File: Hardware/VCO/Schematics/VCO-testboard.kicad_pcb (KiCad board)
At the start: 2 copper layers, 29 parts, among them J1 Conn_01x02, J2 Conn_01x02, J3 Conn_01x02, J4 Conn_01x02, U1 LM358

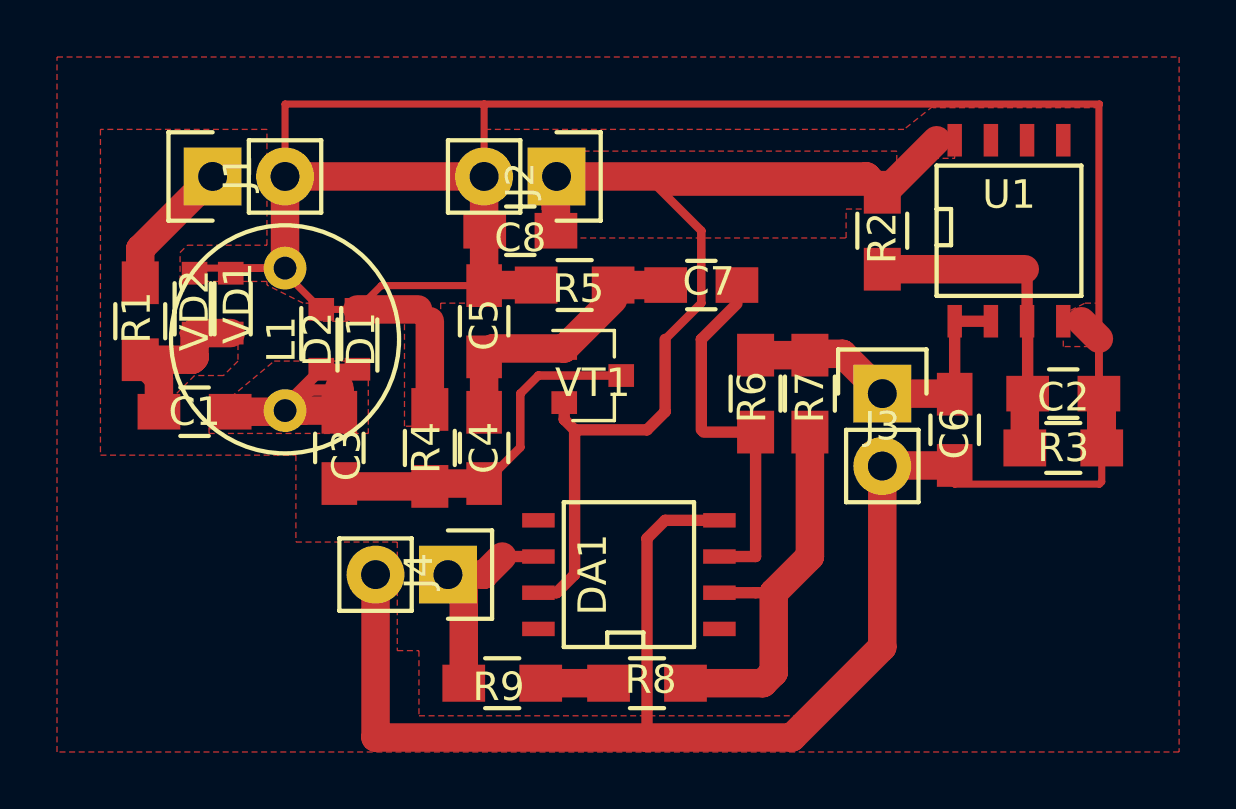
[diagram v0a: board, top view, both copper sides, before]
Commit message: Changed layout a bit
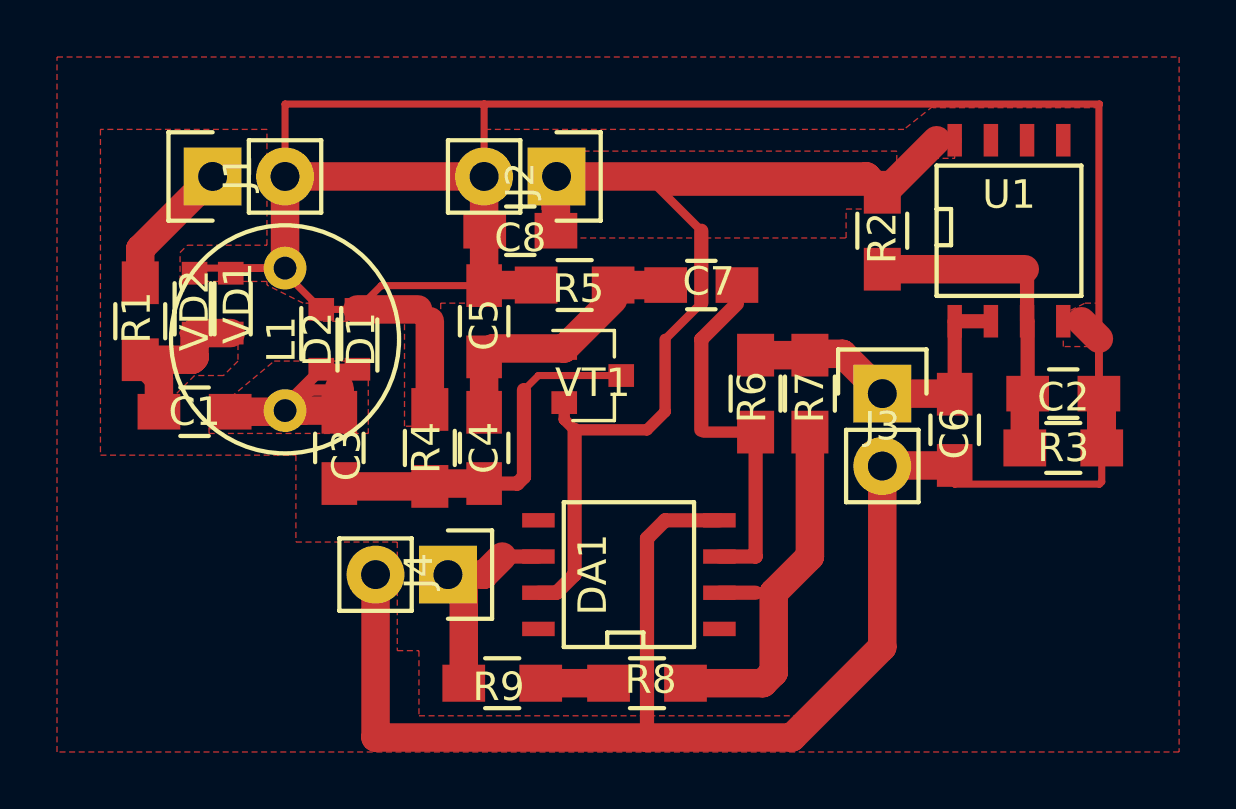
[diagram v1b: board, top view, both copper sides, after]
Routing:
- net Net-(C3-Pad1): track 12.6 -> 13.3 mm
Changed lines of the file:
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@@
     (thickness 1.6)
     (drawings 4)
-    (tracks 163)
+    (tracks 164)
     (zones 0)
     (modules 29)
@@
   )
   (setup
-    (last_trace_width 1)
+    (last_trace_width 0.5)
     (user_trace_width 0.3)
     (user_trace_width 0.4)
+    (user_trace_width 0.5)
     (user_trace_width 1)
     (trace_clearance 0.2)
@@
   (segment (start 16.53 24.23) (end 16.53 25.4) (width 0.25) (layer F.Cu) (net 2))
   (segment (start 17.365 22.64) (end 19.05 22.64) (width 0.25) (layer F.Cu) (net 2))
-  (segment (start 46.99 22.225) (end 46.99 20.32) (width 0.4) (layer F.Cu) (net 3))
+  (segment (start 46.99 22.225) (end 46.99 20.32) (width 0.5) (layer F.Cu) (net 3))
   (segment (start 46.91 20.4) (end 41.91 20.4) (width 1) (layer F.Cu) (net 3))
   (segment (start 46.99 20.32) (end 46.91 20.4) (width 0.25) (layer F.Cu) (net 3))
-  (segment (start 47.01 24.765) (end 47.01 22.245) (width 0.4) (layer F.Cu) (net 3))
+  (segment (start 47.01 24.765) (end 47.01 22.245) (width 0.5) (layer F.Cu) (net 3))
   (segment (start 47.01 22.245) (end 46.99 22.225) (width 0.25) (layer F.Cu) (net 3))
   (segment (start 46.91 24.665) (end 46.91 26.67) (width 1) (layer F.Cu) (net 3))
@@
   (segment (start 24.13 31.115) (end 24.13 36.83) (width 1) (layer F.Cu) (net 4))
   (segment (start 24.13 36.83) (end 33.655 36.83) (width 1) (layer F.Cu) (net 4))
-  (segment (start 36.195 29.21) (end 34.29 29.21) (width 0.4) (layer F.Cu) (net 4))
+  (segment (start 36.195 29.21) (end 34.29 29.21) (width 0.5) (layer F.Cu) (net 4))
   (segment (start 41.91 33.655) (end 41.91 27.305) (width 1) (layer F.Cu) (net 4))
   (segment (start 38.735 36.83) (end 41.91 33.655) (width 1) (layer F.Cu) (net 4))
   (segment (start 33.655 36.83) (end 38.735 36.83) (width 1) (layer F.Cu) (net 4))
-  (segment (start 33.655 29.845) (end 33.655 36.83) (width 0.4) (layer F.Cu) (net 4))
-  (segment (start 34.29 29.21) (end 33.655 29.845) (width 0.4) (layer F.Cu) (net 4))
+  (segment (start 33.655 29.845) (end 33.655 36.83) (width 0.5) (layer F.Cu) (net 4))
+  (segment (start 34.29 29.21) (end 33.655 29.845) (width 0.5) (layer F.Cu) (net 4))
   (segment (start 27.94 14.605) (end 49.53 14.605) (width 0.25) (layer F.Cu) (net 4))
   (segment (start 49.51 14.625) (end 49.51 24.765) (width 0.25) (layer F.Cu) (net 4))
@@
   (segment (start 22.225 21.81) (end 20.955 20.54) (width 0.25) (layer F.Cu) (net 4))
   (segment (start 20.955 20.54) (end 20.955 20.36064) (width 0.25) (layer F.Cu) (net 4))
-  (segment (start 32.75 24.13) (end 29.845 24.13) (width 0.3) (layer F.Cu) (net 5))
-  (segment (start 29.21 26.65) (end 27.94 27.92) (width 0.3) (layer F.Cu) (net 5))
-  (segment (start 29.21 24.765) (end 29.21 26.65) (width 0.3) (layer F.Cu) (net 5))
-  (segment (start 29.845 24.13) (end 29.21 24.765) (width 0.3) (layer F.Cu) (net 5))
+  (segment (start 32.75 24.13) (end 29.845 24.13) (width 0.25) (layer F.Cu) (net 5) (status 400000))
+  (segment (start 29.103 27.92) (end 27.94 27.92) (width 0.5) (layer F.Cu) (net 5) (status 800000))
+  (segment (start 29.337 27.686) (end 29.103 27.92) (width 0.5) (layer F.Cu) (net 5))
+  (segment (start 29.337 24.638) (end 29.337 27.686) (width 0.5) (layer F.Cu) (net 5))
+  (segment (start 29.845 24.13) (end 29.337 24.638) (width 0.25) (layer F.Cu) (net 5))
   (segment (start 27.94 27.92) (end 26.135 27.92) (width 1) (layer F.Cu) (net 5))
   (segment (start 26.135 27.92) (end 26.035 28.02) (width 0.25) (layer F.Cu) (net 5))
@@
   (segment (start 39.45 23.495) (end 39.37 23.415) (width 0.25) (layer F.Cu) (net 7))
   (segment (start 39.37 23.415) (end 37.465 23.415) (width 0.25) (layer F.Cu) (net 7))
-  (segment (start 44.45 24.785) (end 44.45 22.225) (width 0.4) (layer F.Cu) (net 7))
+  (segment (start 44.45 24.785) (end 44.45 22.225) (width 0.5) (layer F.Cu) (net 7))
   (segment (start 44.45 24.785) (end 41.93 24.785) (width 0.25) (layer F.Cu) (net 7))
   (segment (start 41.93 24.785) (end 41.91 24.765) (width 0.25) (layer F.Cu) (net 7))
-  (segment (start 45.72 22.225) (end 44.45 22.225) (width 0.4) (layer F.Cu) (net 7))
-  (segment (start 36.195 30.48) (end 37.465 30.48) (width 0.4) (layer F.Cu) (net 8))
-  (segment (start 37.465 30.48) (end 37.465 26.115) (width 0.4) (layer F.Cu) (net 8))
+  (segment (start 45.72 22.225) (end 44.45 22.225) (width 0.5) (layer F.Cu) (net 7))
+  (segment (start 36.195 30.48) (end 37.465 30.48) (width 0.5) (layer F.Cu) (net 8))
+  (segment (start 37.465 30.48) (end 37.465 26.115) (width 0.5) (layer F.Cu) (net 8))
   (segment (start 36.81 20.955) (end 36.81 21.61) (width 0.25) (layer F.Cu) (net 8))
   (segment (start 35.64 26.115) (end 37.465 26.115) (width 0.4) (layer F.Cu) (net 8))
   (segment (start 35.56 26.035) (end 35.64 26.115) (width 0.3) (layer F.Cu) (net 8))
-  (segment (start 35.56 22.86) (end 35.56 26.035) (width 0.4) (layer F.Cu) (net 8))
-  (segment (start 36.81 21.61) (end 35.56 22.86) (width 0.4) (layer F.Cu) (net 8))
+  (segment (start 35.56 22.86) (end 35.56 26.035) (width 0.5) (layer F.Cu) (net 8))
+  (segment (start 36.81 21.61) (end 35.56 22.86) (width 0.5) (layer F.Cu) (net 8))
+  (segment (start 31.115 26.035) (end 33.655 26.035) (width 0.4) (layer F.Cu) (net 9))
+  (segment (start 35.56 19.05) (end 33.655 17.145) (width 0.3) (layer F.Cu) (net 9))
+  (segment (start 35.56 21.59) (end 35.56 19.05) (width 0.5) (layer F.Cu) (net 9))
+  (segment (start 34.29 22.86) (end 35.56 21.59) (width 0.3) (layer F.Cu) (net 9))
+  (segment (start 34.29 25.4) (end 34.29 22.86) (width 0.4) (layer F.Cu) (net 9))
+  (segment (start 33.655 26.035) (end 34.29 25.4) (width 0.4) (layer F.Cu) (net 9))
   (segment (start 30.48 17.145) (end 41.355 17.145) (width 1) (layer F.Cu) (net 9))
   (segment (start 41.355 17.145) (end 41.91 17.7) (width 1) (layer F.Cu) (net 9))
   (segment (start 30.46 19.05) (end 30.46 17.165) (width 1) (layer F.Cu) (net 9))
   (segment (start 30.46 17.165) (end 30.48 17.145) (width 1) (layer F.Cu) (net 9))
-  (segment (start 29.845 31.75) (end 30.48 31.75) (width 0.4) (layer F.Cu) (net 9))
-  (segment (start 31.115 31.115) (end 31.115 26.035) (width 0.4) (layer F.Cu) (net 9))
-  (segment (start 30.48 31.75) (end 31.115 31.115) (width 0.4) (layer F.Cu) (net 9))
+  (segment (start 29.845 31.75) (end 30.48 31.75) (width 0.5) (layer F.Cu) (net 9))
+  (segment (start 31.115 31.115) (end 31.115 26.035) (width 0.5) (layer F.Cu) (net 9))
+  (segment (start 30.48 31.75) (end 31.115 31.115) (width 0.5) (layer F.Cu) (net 9))
   (segment (start 41.91 17.7) (end 34.21 17.7) (width 0.25) (layer F.Cu) (net 9))
   (segment (start 34.21 17.7) (end 33.655 17.145) (width 0.25) (layer F.Cu) (net 9))
   (segment (start 41.91 17.7) (end 41.99 17.7) (width 0.25) (layer F.Cu) (net 9))
   (segment (start 41.99 17.7) (end 43.815 15.875) (width 1) (layer F.Cu) (net 9))
-  (segment (start 43.815 15.875) (end 44.45 15.875) (width 0.25) (layer F.Cu) (net 9))
+  (segment (start 43.815 15.875) (end 44.45 15.875) (width 0.5) (layer F.Cu) (net 9))
   (segment (start 30.46 19.05) (end 30.46 17.165) (width 0.25) (layer F.Cu) (net 9))
   (segment (start 30.46 17.165) (end 30.48 17.145) (width 0.25) (layer F.Cu) (net 9))
   (segment (start 30.75 25.08) (end 30.75 25.67) (width 0.4) (layer F.Cu) (net 9))
   (segment (start 30.75 25.67) (end 31.115 26.035) (width 0.4) (layer F.Cu) (net 9))
-  (segment (start 31.115 26.035) (end 33.655 26.035) (width 0.4) (layer F.Cu) (net 9))
-  (segment (start 33.655 26.035) (end 34.29 25.4) (width 0.4) (layer F.Cu) (net 9))
-  (segment (start 34.29 25.4) (end 34.29 22.86) (width 0.4) (layer F.Cu) (net 9))
-  (segment (start 34.29 22.86) (end 35.56 21.59) (width 0.3) (layer F.Cu) (net 9))
-  (segment (start 35.56 21.59) (end 35.56 19.05) (width 0.3) (layer F.Cu) (net 9))
-  (segment (start 35.56 19.05) (end 33.655 17.145) (width 0.3) (layer F.Cu) (net 9))
   (segment (start 33.655 17.145) (end 30.48 17.145) (width 0.25) (layer F.Cu) (net 9))
   (segment (start 27.225 34.925) (end 27.225 31.67) (width 1) (layer F.Cu) (net 10))
   (segment (start 27.225 31.67) (end 26.67 31.115) (width 0.25) (layer F.Cu) (net 10))
   (segment (start 26.67 31.115) (end 27.94 31.115) (width 1) (layer F.Cu) (net 10))
-  (segment (start 28.575 30.48) (end 29.845 30.48) (width 0.4) (layer F.Cu) (net 10))
+  (segment (start 28.575 30.48) (end 29.845 30.48) (width 0.5) (layer F.Cu) (net 10))
   (segment (start 27.94 31.115) (end 28.575 30.48) (width 1) (layer F.Cu) (net 10))
   (segment (start 35.005 34.925) (end 37.719 34.925) (width 1) (layer F.Cu) (net 11))
@@
   (segment (start 39.37 26.115) (end 39.37 30.48) (width 1) (layer F.Cu) (net 11))
   (segment (start 38.1 31.75) (end 37.465 31.75) (width 0.4) (layer F.Cu) (net 11))
-  (segment (start 37.465 31.75) (end 36.195 31.75) (width 0.4) (layer F.Cu) (net 11))
+  (segment (start 37.465 31.75) (end 36.195 31.75) (width 0.5) (layer F.Cu) (net 11))
   (segment (start 39.37 30.48) (end 38.1 31.75) (width 1) (layer F.Cu) (net 11))
   (segment (start 15.875 20.875) (end 15.875 19.685) (width 1) (layer F.Cu) (net 12))
